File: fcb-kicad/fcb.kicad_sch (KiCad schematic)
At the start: 52 parts, among them J1 Conn_ESC_4in1, J2 SWD, SW1 SW_Push, SW2 SW_SPDT, U1 TPS5430DDA, U2 AMS1117-3.3, U5 STM32F411CEUx, Y1 16 MHz

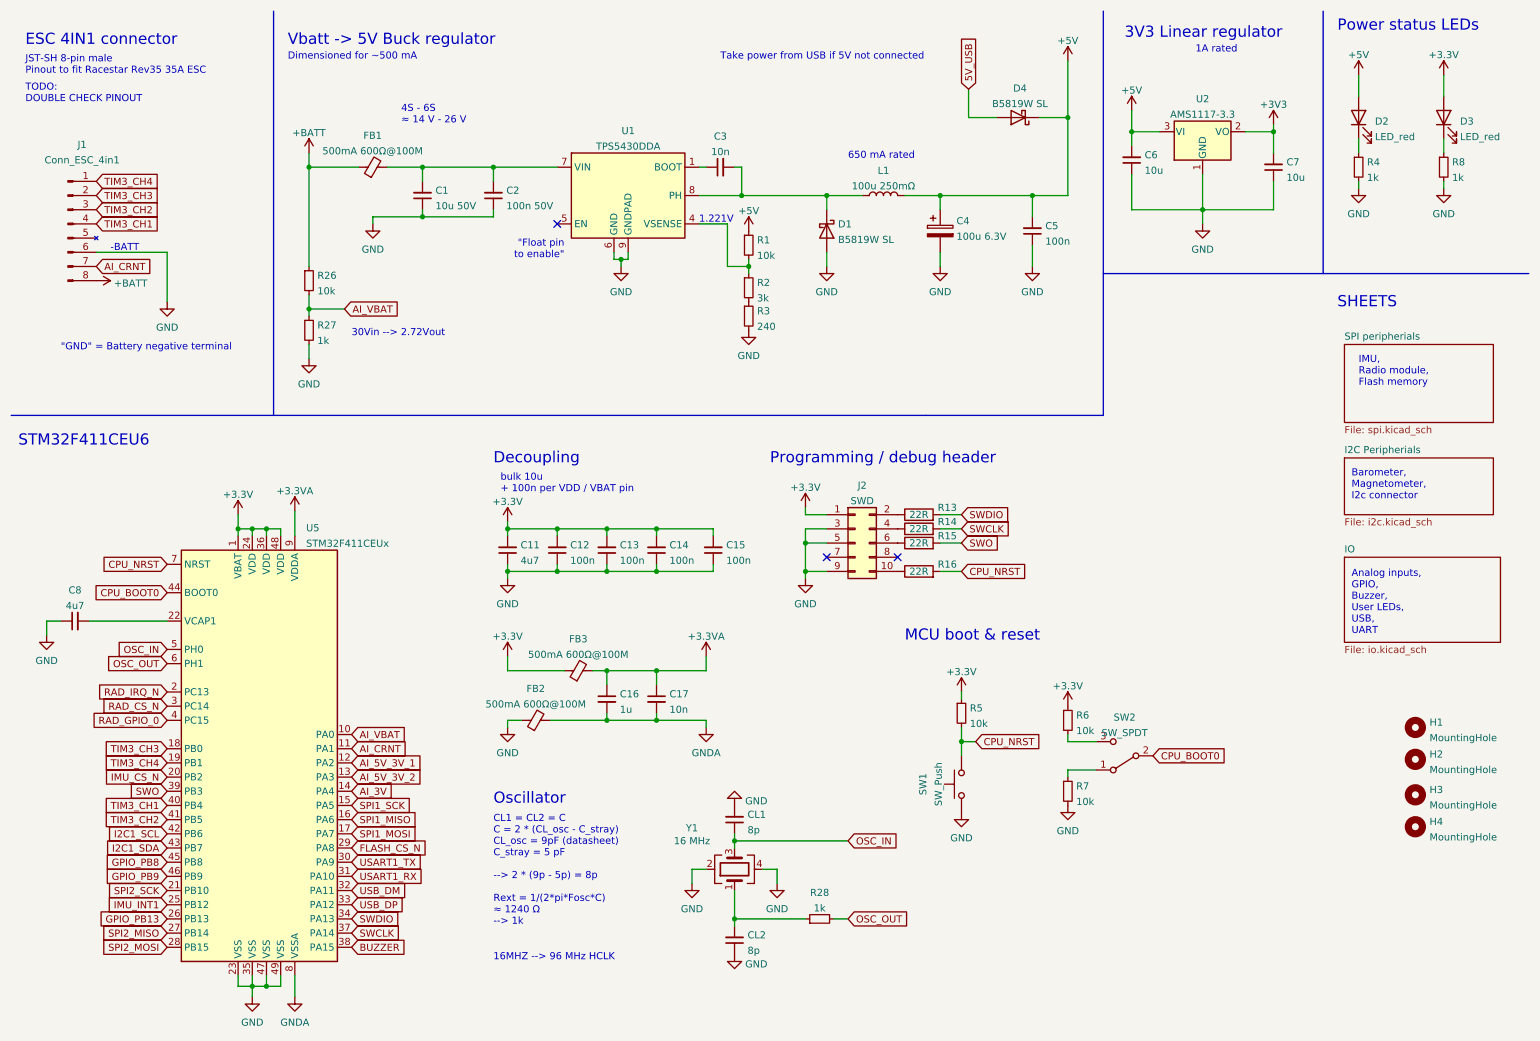
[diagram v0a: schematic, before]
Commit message: Schema rev0 done, Layout components grouped
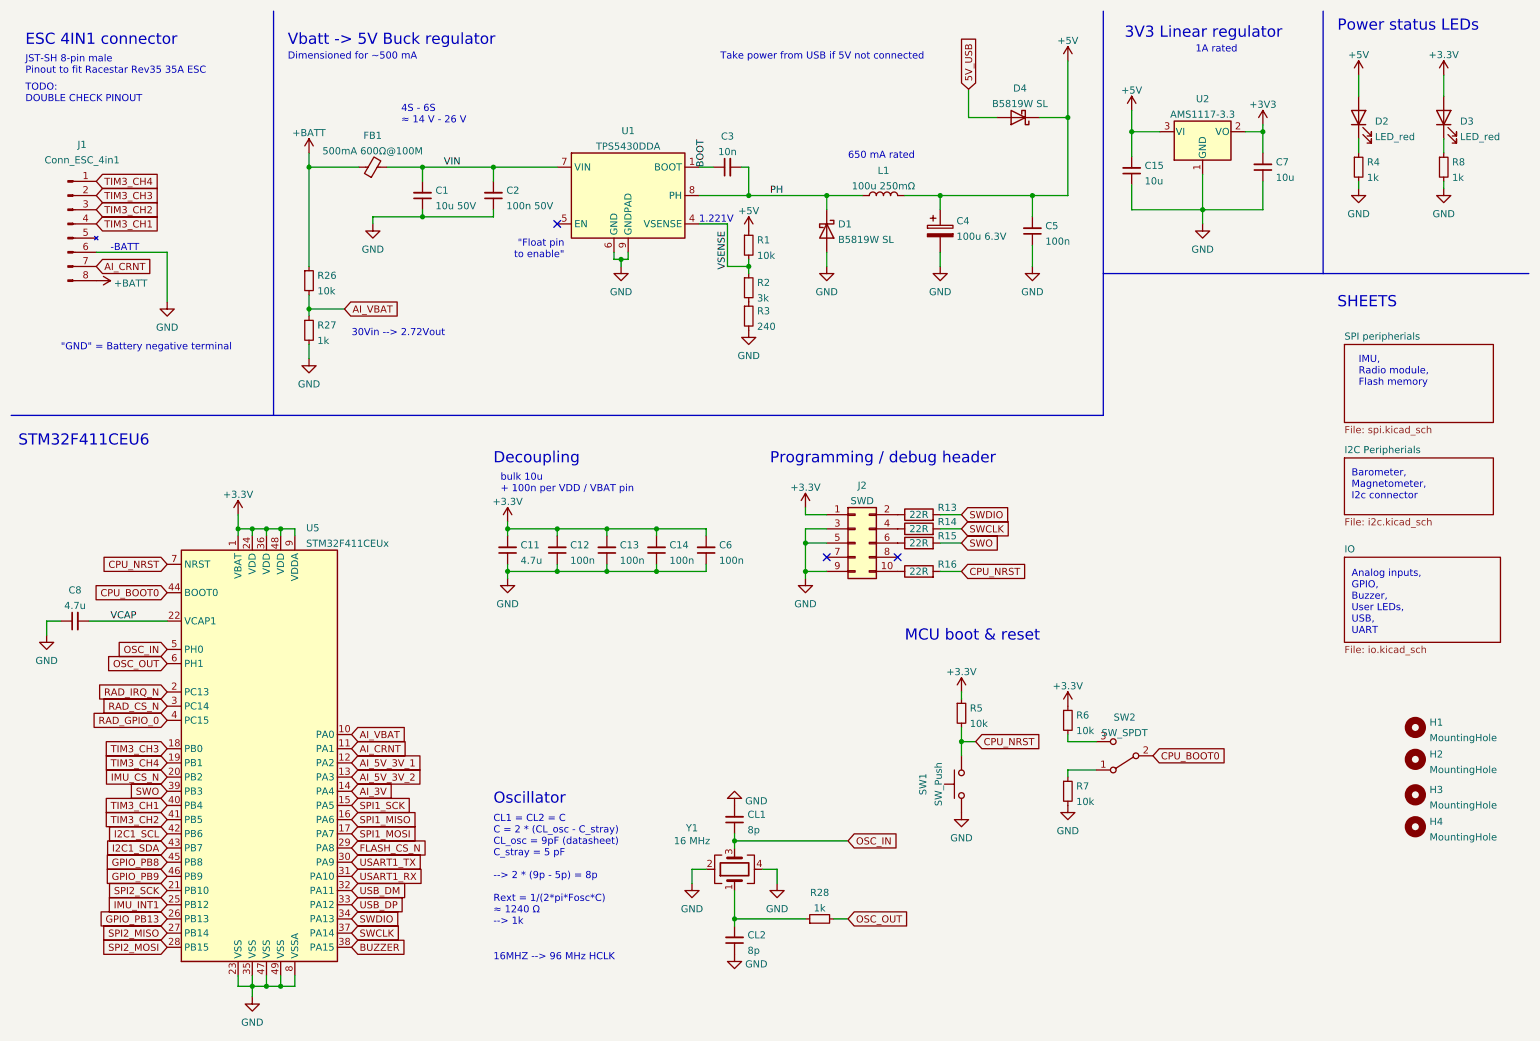
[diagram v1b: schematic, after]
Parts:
- removed C16: 1u, symbol Device:C_Small
- removed C17: 10n, symbol Device:C_Small
- removed FB2, FB3: 500mA 600Ω@100M, Capacitor_SMD:C_0805_2012Metric, symbol Device:FerriteBead_Small
- C11, C8: value 4u7 -> 4.7u
- C15: value 100n -> 10u; LCSC C14663 -> C13585
- C6: value 10u -> 100n; LCSC C13585 -> C14663
- CL1, CL2: footprint (none) -> Capacitor_SMD:C_0603_1608Metric
- J1: footprint (none) -> Connector_JST:JST_SH_SM08B-SRSS-TB_1x08-1MP_P1.00mm_Horizontal
- J2: footprint (none) -> Connector_PinHeader_1.27mm:PinHeader_2x05_P1.27mm_Vertical
- R13, R14, R15, R16, R27, R28, R4, R8: footprint (none) -> Resistor_SMD:R_0603_1608Metric
- SW1: footprint (none) -> 000_sjt:Button-2.9x4.0mm-SMD; LCSC (none) -> C720477
- SW2: footprint (none) -> 000_sjt:DIP_SPDT
- U1: footprint Package_SO:TI_SO-PowerPAD-8_ThermalVias -> Package_SO:TI_SO-PowerPAD-8
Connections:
- net +3.3VA is gone; now on net +3V3: U5.9 (VDDA)
- net GNDA is gone; now on net GND: U5.8 (VSSA)
- net +3V3: now also C6.2; no longer C15.2
- net +5V: now also C15.2; no longer C6.2
- net BOOT: now reaches C3.1, U1.1 (BOOT)
- net VSENSE: now reaches R1.2, R2.1, U1.4 (VSENSE)
- net VIN: now reaches C1.2, C2.2, FB1.2, U1.7 (VIN)
- net PH: now reaches C3.2, D1.1 (K), L1.1, U1.8 (PH)
- net VCAP: now reaches C8.2, U5.22 (VCAP1)
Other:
- moved on the sheet: C3, C7

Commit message: PCB rev0: "Babby's first Leiska"
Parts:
- removed R6: 10k, Resistor_SMD:R_0603_1608Metric, symbol Device:R_Small
- removed SW2: SW_SPDT, 000_sjt:DIP_SPDT, symbol Switch:SW_SPDT
- U2: renamed from U1; footprint Package_SO:TI_SO-PowerPAD-8 -> Package_SO:TI_SO-PowerPAD-8_ThermalVias
- renumbered C8 to C1, C5 to C10, C4 to C11, C15 to C12, C7 to C13, C1 to C2, C2 to C3, C11 to C4, C12 to C5, C13 to C6, C14 to C7, C6 to C8, C3 to C9, D4 to D2, D2 to D3, D3 to D4, R26 to R1, R16 to R10, R5 to R11, R7 to R13, R4 to R14, R8 to R15, R27 to R2, R1 to R3, R2 to R4, R3 to R5, R28 to R6, R13 to R7, R14 to R8, R15 to R9, U5 to U1, U2 to U3
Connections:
- net CPU_BOOT0: now also R13.1
- net OSC_OUT_R: now reaches CL2.2, R6.1, Y1.1
- net USB_DM renamed USB_D-
- net USB_DP renamed USB_D+
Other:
- note added: "No need for boot switch, programming done via SWD"
- note added: "bulk + 100n per VDD / VBAT pin"
- note removed: "bulk 10u + 100n per VDD / VBAT pin"
- moved on the sheet: C10, C11, CL2, R6

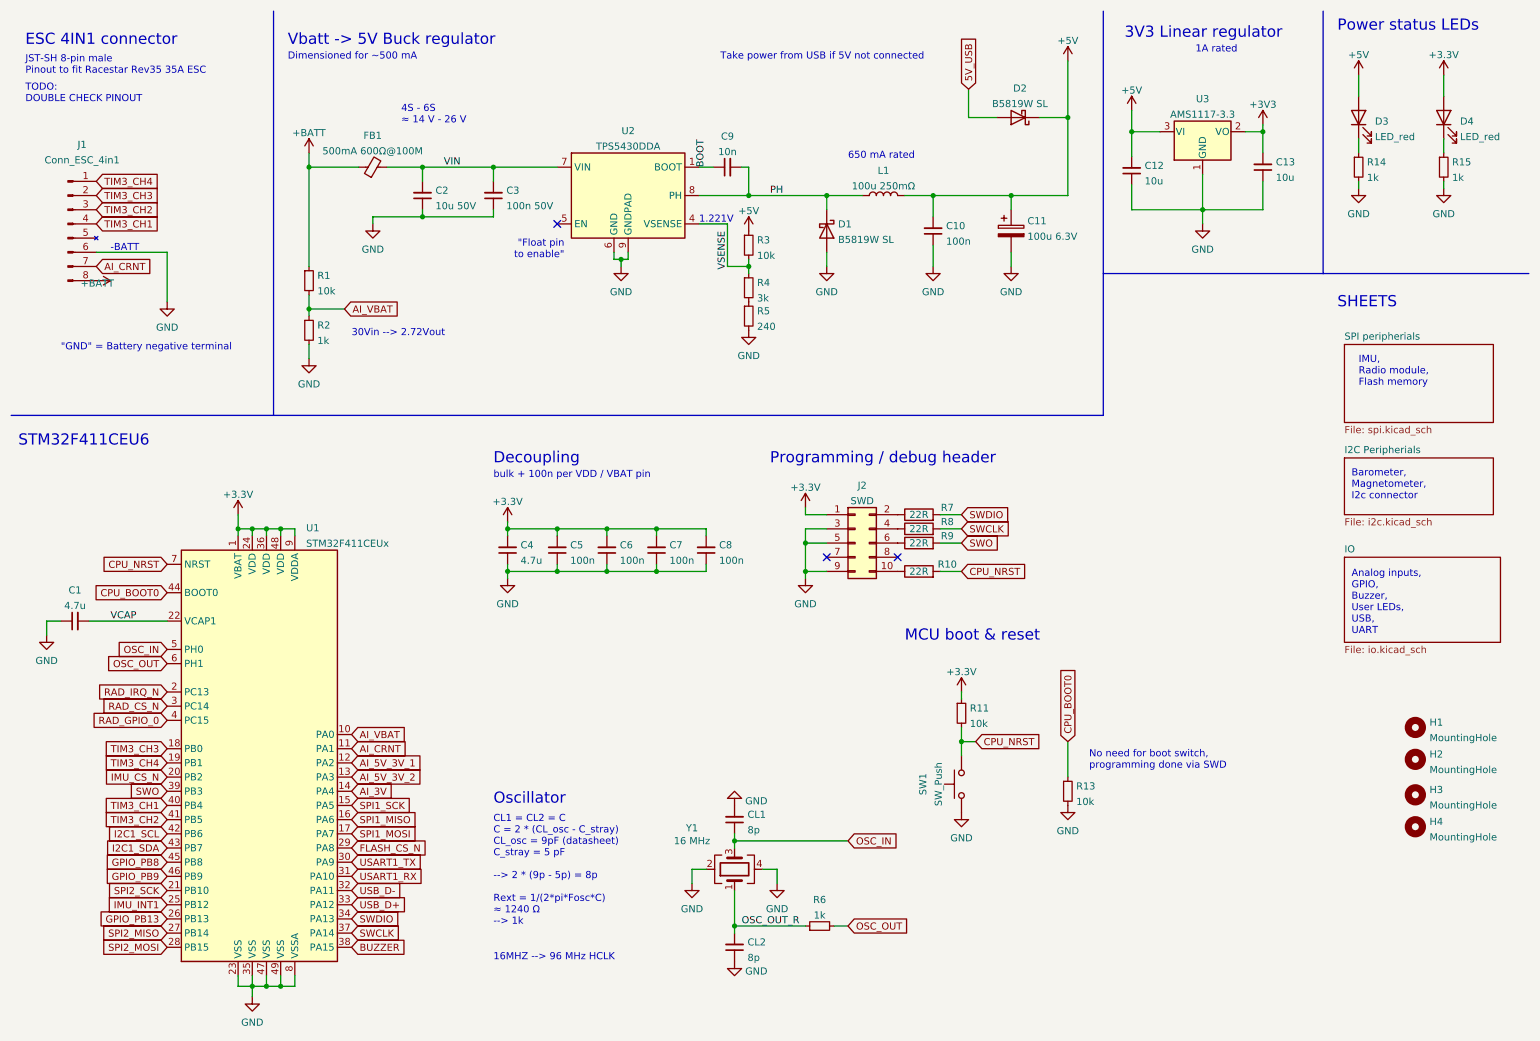
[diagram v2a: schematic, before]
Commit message: Less routing on inner layers, fabrication, BOM should be OK
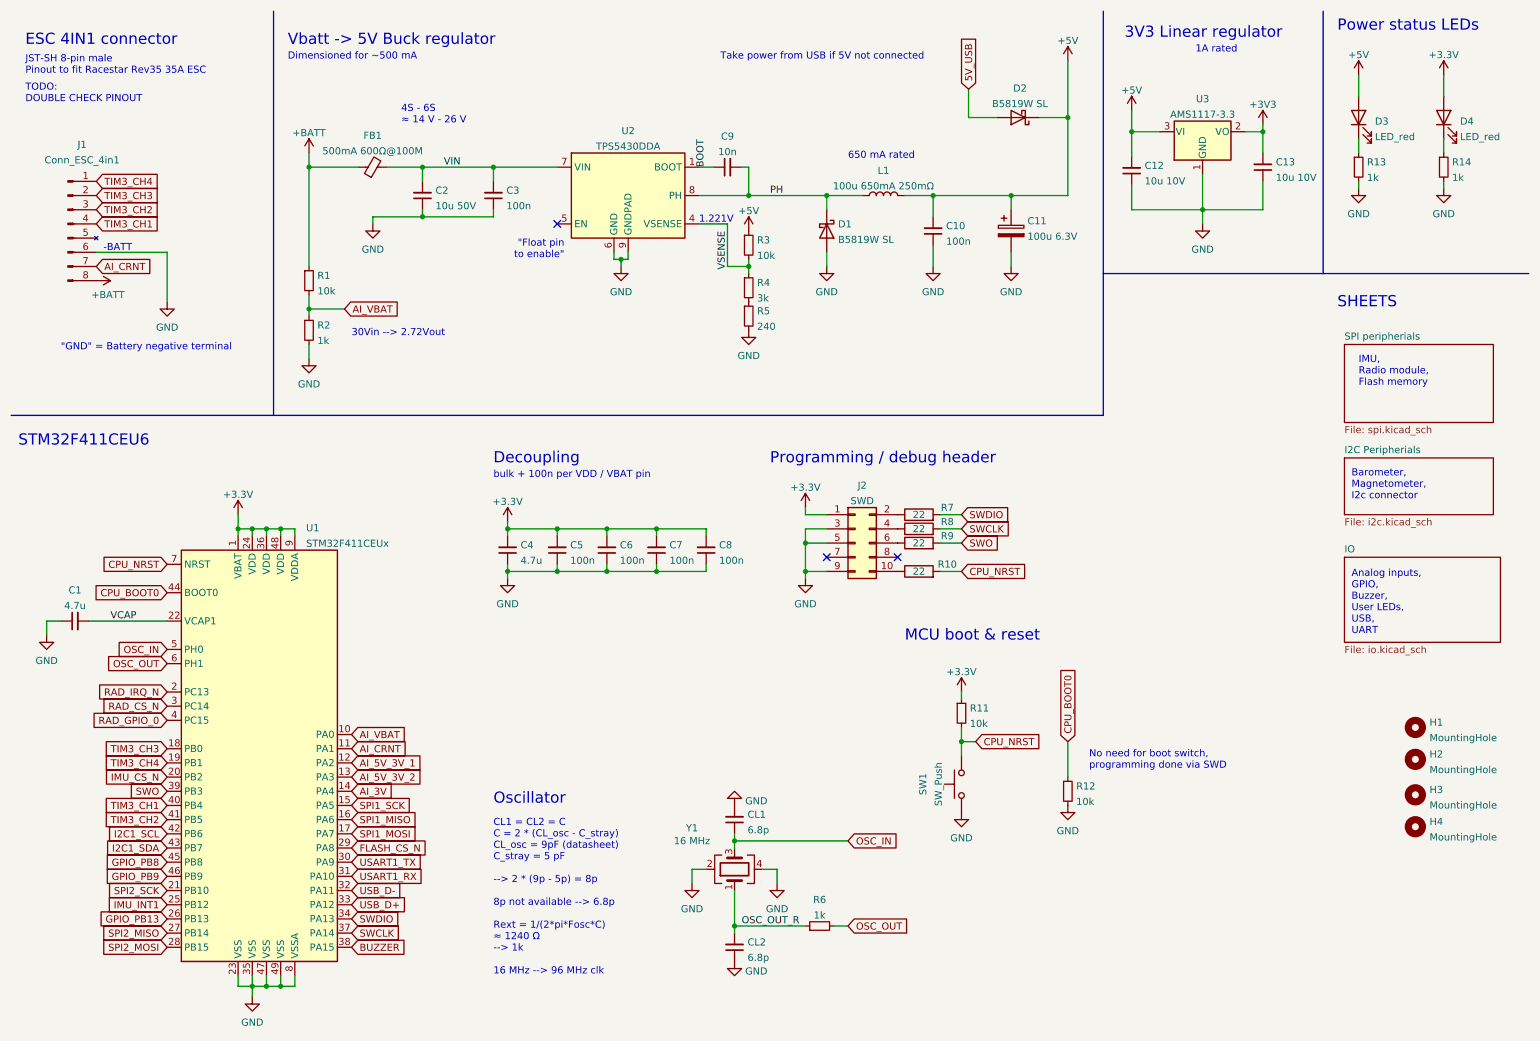
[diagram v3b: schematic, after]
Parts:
- C1, C4: LCSC (none) -> C19666
- C12, C13: value 10u -> 10u 10V; LCSC C13585 -> C19702
- C2: LCSC C13585 -> C89632
- C3: value 100n 50V -> 100n
- CL1, CL2: value 8p -> 6.8p; LCSC (none) -> C1679
- D3, D4: LCSC C2286 -> C84263
- FB1: LCSC (none) -> C1017
- J1: LCSC (none) -> C49633
- J2: LCSC (none) -> C2895038
- L1: value 100u 250mΩ -> 100u 650mA 250mΩ
- R10, R7, R8, R9: value 22R -> 22; LCSC (none) -> C23345
- R13: renamed from R14; LCSC (none) -> C21190
- R14: renamed from R15; LCSC (none) -> C21190
- R2, R6: LCSC (none) -> C21190
- U1: LCSC (none) -> C60420
- renumbered R13 to R12
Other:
- note added: "CL1 = CL2 = C C = 2 * (CL_osc - C_stray) CL_osc = 9pF (datasheet) C_stray = 5 pF --> 2 * (9p - 5p) = 8p 8p not available --> 6.8p Rext = 1/(2*pi*Fosc*C) ≈ 1240 Ω --> 1k 16 MHz --> 96 MHz clk"
- note removed: "16MHZ --> 96 MHz HCLK"
- note removed: "CL1 = CL2 = C C = 2 * (CL_osc - C_stray) CL_osc = 9pF (datasheet) C_stray = 5 pF --> 2 * (9p - 5p) = 8p Rext = 1/(2*pi*Fosc*C) ≈ 1240 Ω --> 1k"

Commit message: Change MCU to STM32F411CCU6
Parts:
- U1: symbol MCU_ST_STM32F4:STM32F411CEUx -> MCU_ST_STM32F4:STM32F411CCUx
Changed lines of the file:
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@@
     (pin "9")
   )
-  (symbol (lib_id "MCU_ST_STM32F4:STM32F411CEUx") (at 58.42 144.78 0) (unit 1)
+  (symbol (lib_id "MCU_ST_STM32F4:STM32F411CCUx") (at 58.42 144.78 0) (unit 1)
     (in_bom yes) (on_board yes) (fields_autoplaced)
     (property "Reference" "U1" (id 0) (at 65.5194 105.2535 0)
